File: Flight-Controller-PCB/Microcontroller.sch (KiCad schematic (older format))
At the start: 37 parts, among them J9 USB_B_Micro, Q3 Q_PMOS_GSD, Q4 Q_PMOS_GSD, SW1 Push-Switch, U3 ATmega32U4-AU, U4 NCP1117-5.0, U5 LP2985-3.3, Y1 16MHz, CL 7pF

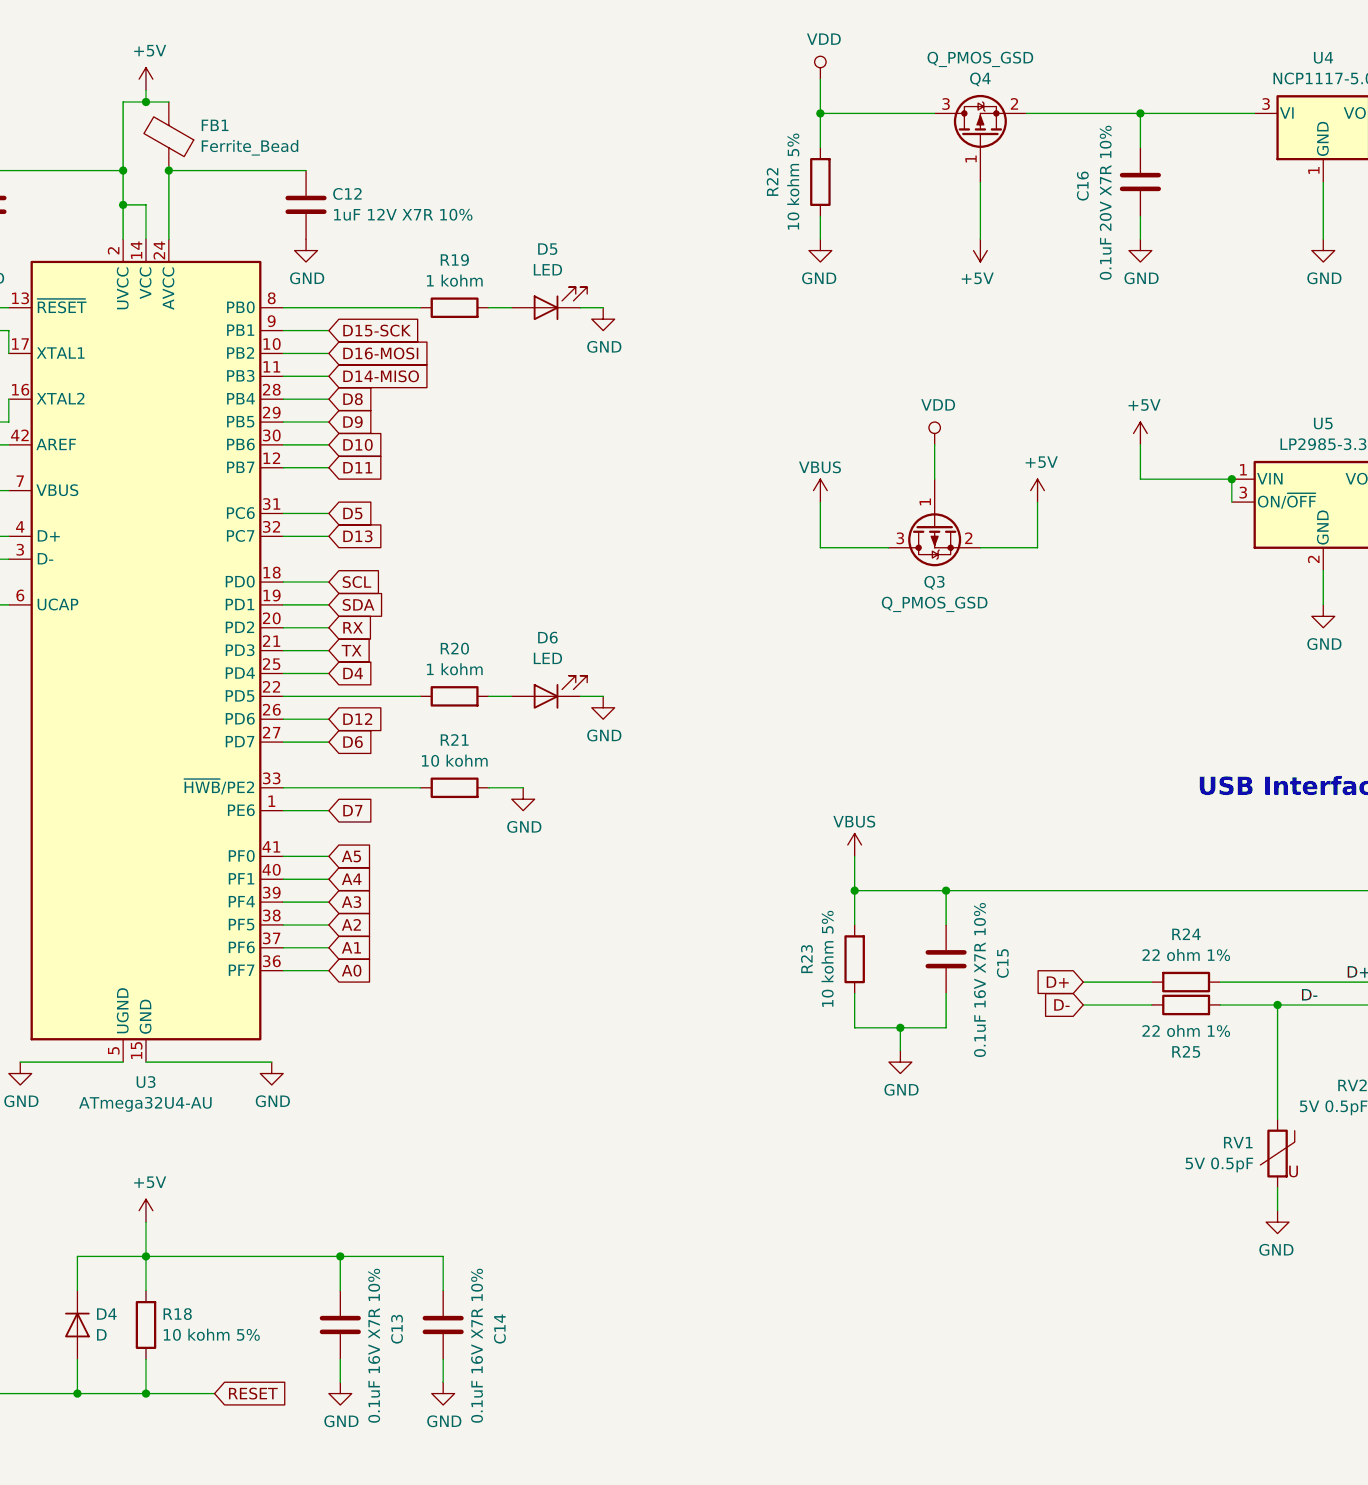
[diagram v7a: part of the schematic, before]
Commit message: Main page and IMU reviewed and passed
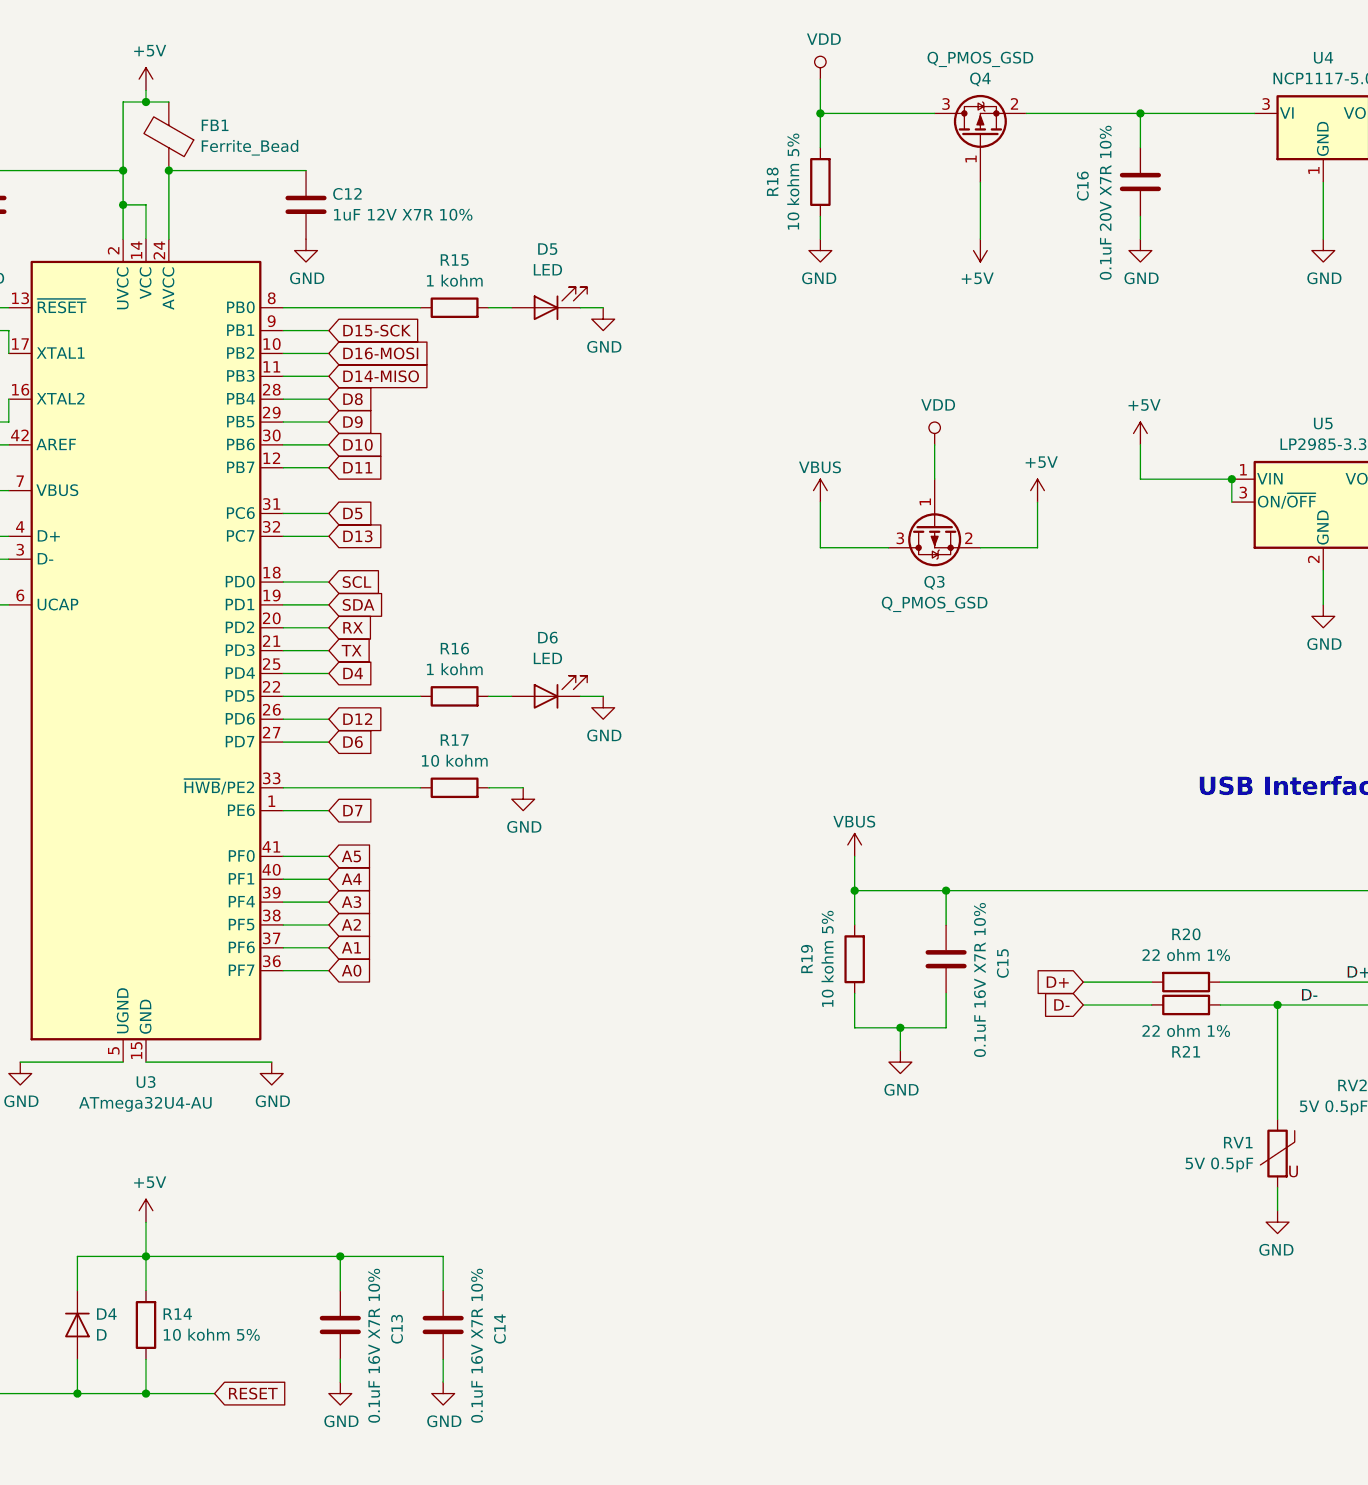
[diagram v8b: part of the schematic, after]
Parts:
- renumbered R18 to R14, R19 to R15, R20 to R16, R21 to R17, R22 to R18, R23 to R19, R24 to R20, R25 to R21
